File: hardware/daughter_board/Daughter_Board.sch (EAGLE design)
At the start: 75 parts, among them IC1 LMV358MMX, IC2 LMV358MMX, IC3 ATMEGA2560-16AU, IC4 ATMEGA16U2-MU, IC5 LMV358MMX, IC6 LP2985-33DBVR, IC7 LMV358IDGKR, IC8 LMV358MMX, IC9 LMV358MMX, J1 USB_MINI-B_SMT, T1 FDN340P, Y1 CSTCE16M0V53-R0 16MHZ, Y2 16MHz

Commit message: partial implementation of daughter board with rpi as bootloader
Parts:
- removed C10, C13: 1u, SmartPrj:C-EU0603-RND
- removed C11, C12, C6, C7, C8, C9: 100n, SmartPrj:C-EU0603-RND
- removed C14, C15: 22p, SmartPrj:C-EU0603-RND
- removed D2: CD1206-S01575, diode:DIODE-MINIMELF
- removed F1: MF-MSMF050-2 500mA, rcl:L-EUL1812
- removed GROUND, RESET-EN: (no value), jumper:SJ
- removed IC4: ATMEGA16U2-MU, SmartPrj:ATMEGA16U2-MU
- removed IC6: LP2985-33DBVR, SmartPrj:LP2985-XXDBVR33
- removed IC7: LMV358IDGKR, linear:LMV358MMX
- removed ICSP1: 3x2M, SmartPrj:PINHD-2X3
- removed JP2: (no value), adafruit:PINHD-1X12-CB
- removed JP5: 2x2M - NM, SmartPrj:PINHD-2X2
- removed ON: GREEN, led:LEDCHIP-LED0805
- removed RN1, RN10, RN11, RN3, RN4, RN6, RN8, RN9: 1k, resistor-dil:4R-NCAY16
- removed RN2: 22R, resistor-dil:4R-NCAY16
- removed RN5, RN7: 10K, resistor-dil:4R-NCAT16
- removed RX, TX: YELLOW, led:LEDCHIP-LED0805
- removed T1: FDN340P, zetex:PMOSSOT23
- removed Y2: 16MHz, SmartPrj:XTAL/S
- removed Z1, Z2: CG0603MLC-05E, varistor:VARISTORCN0603
- added J3, J4: (no value), SparkFun-Connectors:CONN_03
- added J5: (no value), SparkFun-Connectors:CONN_04
- added Q1: BSS138, SparkFun:MOSFET-NCHANNELSMD
- added R10, R11, R12, R3, R4, R5, R6, R7, R8, R9: 1k, resistor:R-EU_R0603
- added R13, R14, R15, R16, R17, R18, R19: 10k, resistor:R-EU_R0603
- added R20, R21: 10K, SparkFun:RESISTOR0603-RES
- J1: value USB_MINI-B_SMT -> (none); device SparkFun-Connectors:USB_MINI-B_SMT -> SparkFun-Connectors:CONN_03
- J2: device SparkFun-Connectors:CONN_04 -> SparkFun-Connectors:CONN_03
- L1: value BLM21 -> GREEN; device wuerth-elektronik:WE-CBF_0805 -> led:LEDCHIP-LED0805
- R2: value 1M -> 1k; device SmartPrj:R-EU_R0603 -> resistor:R-EU_R0603
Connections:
- removed net +3V3: C13.2, IC6.OUT, IC7B.-IN
- removed net 3V3_OUT_2: RPI-ZERO.17
- removed net 8PB4: IC4.(T1/PCINT4)PB4, JP5.1
- removed net 8PB5: IC4.(PCINT5)PB5, JP5.3
- removed net 8PB6: IC4.(PCINT6)PB6, JP5.2
- removed net 8PB7: IC4.(PCINT7/OC0A/OC1C)PB7, JP5.4
- removed net AREF: C3.1, IC3.AREF
- removed net CMP: C12.2, IC7B.+IN, RN5C.2, RN5D.2
- removed net D+: J1.D+, RN2A.2, Z2.2
- removed net D-: J1.D-, RN2D.2, Z1.2
- removed net DTR: C7.1, IC4.(CTS/HWB/AIN6/TO/INT7)PD7, RN3D.1
- removed net GATE_CMD: IC7B.OUT, T1.G
- removed net M8RXD: IC4.(TXD1/INT3)PD3, RN4B.2
- removed net M8TXD: IC4.(RXD1/AIN1/INT2)PD2, RN4A.2
- removed net MISO2: IC4.(PD0/MISO/PCINT3)PB3, ICSP1.1
- removed net MOSI2: IC4.(PDI/MOSI/PCINT2)PB2, ICSP1.4
- removed net N$54: RN4D.1, RX.A
- removed net N$55: RN4C.1, TX.A
- removed net PA0: IC3.(AD0)PA0
- removed net PA1: IC3.(AD1)PA1
- removed net PA2: IC3.(AD2)PA2
- removed net PA3: IC3.(AD3)PA3
- removed net PA4: IC3.(AD4)PA4
- removed net PA5: IC3.(AD5)PA5
- removed net PA6: IC3.(AD6)PA6
- removed net PA7: IC3.(AD7)PA7
- removed net PB0: IC3.(SS/PCINT0)PB0
- removed net PB4: IC3.(OC2A/PCINT4)PB4
- removed net PB5: IC3.(OC1A/PCINT5)PB5
- removed net PB6: IC3.(OC1B/PCINT6)PB6
- removed net PB7: IC3.(OC0A/OC1C/PCINT7)PB7
- removed net PC0: IC3.(A8)PC0
- removed net PC1: IC3.(A9)PC1
- removed net PC2: IC3.(A10)PC2
- removed net PC3: IC3.(A11)PC3
- removed net PC4: IC3.(A12)PC4
- removed net PC5: IC3.(A13)PC5
- removed net PC6: IC3.(A14)PC6
- removed net PC7: IC3.(A15)PC7
- removed net PD7: IC3.(T0)PD7
- removed net PF0: IC3.(ADC0)PF0
- removed net PF1: IC3.(ADC1)PF1
- removed net PF3: IC3.(ADC3)PF3
- removed net PF7: IC3.(ADC7/TDI)PF7
- removed net PG0: IC3.(WR)PG0
- removed net PG1: IC3.(RD)PG1
- removed net PG2: IC3.(ALE)PG2
- removed net PH3: IC3.PH3(OC4A)
- removed net PH4: IC3.PH4(OC4B)
- removed net PL0: IC3.PL0(ICP4)
- removed net PL1: IC3.PL1(ICP5)
- removed net PL2: IC3.PL2(T5)
- removed net PL3: IC3.PL3(OC5A)
- removed net PL4: IC3.PL4(OC5B)
- removed net PL5: IC3.PL5(OC5C)
- removed net PL6: IC3.PL6
- removed net PL7: IC3.PL7
- removed net RD+: IC4.D+, RN2A.1
- removed net RD-: IC4.D-, RN2D.1
- removed net RESET2: D2.A, IC4.RESET(PC1/DW), ICSP1.5, RN5B.2
- removed net RXL: IC4.(INT5/AIN3)PD4, RX.C
- removed net SCK2: IC4.(SCLK/PCINT1)PB1, ICSP1.3
- removed net TXL: IC4.(XCK/AIN4/PCINT12)PD5, TX.C
- removed net UGND: C10.2, GROUND.1, IC4.UGND, J1.GND, L1.1
- removed net USBVCC: C8.1, F1.1, IC4.UVCC, T1.D
- removed net USHIELD: J1.SHIELD, L1.2, Z1.1, Z2.1
- removed net VIN: RN5C.1
- removed net VUCAP: C10.1, IC4.UCAP
- removed net XT1: C14.1, IC4.XTAL1, R2.1, Y2.2
- removed net XT2: C15.1, IC4.XTAL2(PC0), R2.2, Y2.1
- removed net XVCC: F1.2, J1.VBUS
- new net HV: R21.1
- new net HV1: Q1.D, R21.2
- new net LV: Q1.G, R20.1
- new net LV1: Q1.S, R20.2
- net +5V: now also C3.1, J5.4, R12.1, R13.1; no longer C11.2, C6.1, C9.1, D2.C, IC4.AVCC, IC4.VCC, IC6.IN, IC6.ON/!OFF, IC7P.V+, ICSP1.2, J2.4, RN3A.1, RN4C.2, RN4D.2, RN5A.1, RN5B.1, T1.S
- net 3V3_OUT: now also R14.1, R15.1, R16.1, R17.1, R18.1, R19.1, RPI-ZERO.17; no longer RN7B.2, RN7C.2
- net GND: now also J1.1, J2.1, J3.1, J4.1, J5.2, L1.C; no longer C11.1, C12.1, C13.1, C14.2, C15.2, C6.2, C8.2, C9.2, GROUND.2, IC4.GND, IC4.PAD, IC6.GND, IC7P.V-, ICSP1.6, J2.2, JP2.12, JP2.3, JP2.4, JP2.9, ON.C, RN11A.1, RN11B.1, RN11C.1, RN11D.1, RN3D.2, RN5D.1
- net GPIO14: now also R14.2; no longer RN11A.2
- net GPIO15: now also R16.2; no longer RN11C.2
- net GPIO18: now also R17.2; no longer RN11D.2
- net GPIO4: now also R15.2; no longer RN11B.2
- net N$1: now also R3.2; no longer RN1A.2
- net N$10: now also R4.2; no longer RN6A.1
- net N$11: now also R5.2; no longer RN6B.1
- net N$12: now also R11.1; no longer RN9A.2
- net N$13: now also R7.2; no longer RN8B.2
- net N$14: now also R6.2; no longer RN8A.2
- net N$15: now also R10.1; no longer RN9B.2
- net N$16: now also R8.1; no longer RN10A.2
- net N$17: now also R9.1; no longer RN10B.2
- net N$18: now also R9.2; no longer RN10B.1
- net N$19: now also R8.2; no longer RN10A.1
- net N$2: now also R2.2; no longer RN1B.2
- net N$21: now also R11.2; no longer RN9A.1
- net N$22: now also R10.2; no longer RN9B.1
- net N$3: now also L1.A, R12.2; no longer ON.A, RN3A.2
- net N$4: now also R2.1; no longer RN1B.1
- net N$5: now also R7.1; no longer RN8B.1
- net N$6: now also R3.1; no longer RN1A.1
- net N$7: now also R6.1; no longer RN8A.1
- net N$8: now also R5.1; no longer RN6B.2
- net N$9: now also R4.1; no longer RN6A.2
- net PE0: now also J4.3; no longer JP2.10, RN4B.1
- net PE1: now also J4.2; no longer JP2.11, RN4A.1
- net PH5: now also IC1A.+IN, J5.1; no longer IC1B.+IN, J2.1
- net PH6: now also IC1B.+IN, J5.3; no longer IC1A.+IN, J2.3
- net RESET: now also R13.2; no longer C7.2, RESET-EN.1, RESET-EN.2, RN5A.2
- net RXD1: now also J3.3; no longer JP2.6
- net RXD2: now also J2.3; no longer JP2.7
- net RXD3: now also J1.3; no longer JP2.1
- net SCL: now also R18.2; no longer IC3.(SCL/INT0)PD0, RN7B.1
- net SDA: now also R19.2; no longer IC3.(SDA/INT1)PD1, RN7C.1
- net TXD1: now also J3.2; no longer JP2.5
- net TXD2: now also J2.2; no longer JP2.8
- net TXD3: now also J1.2; no longer JP2.2
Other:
- note removed: "USB boot En"
- moved on the sheet: C1, C2, C3, IC8A, L8, PAD1, PAD2, R1, R2, RESET

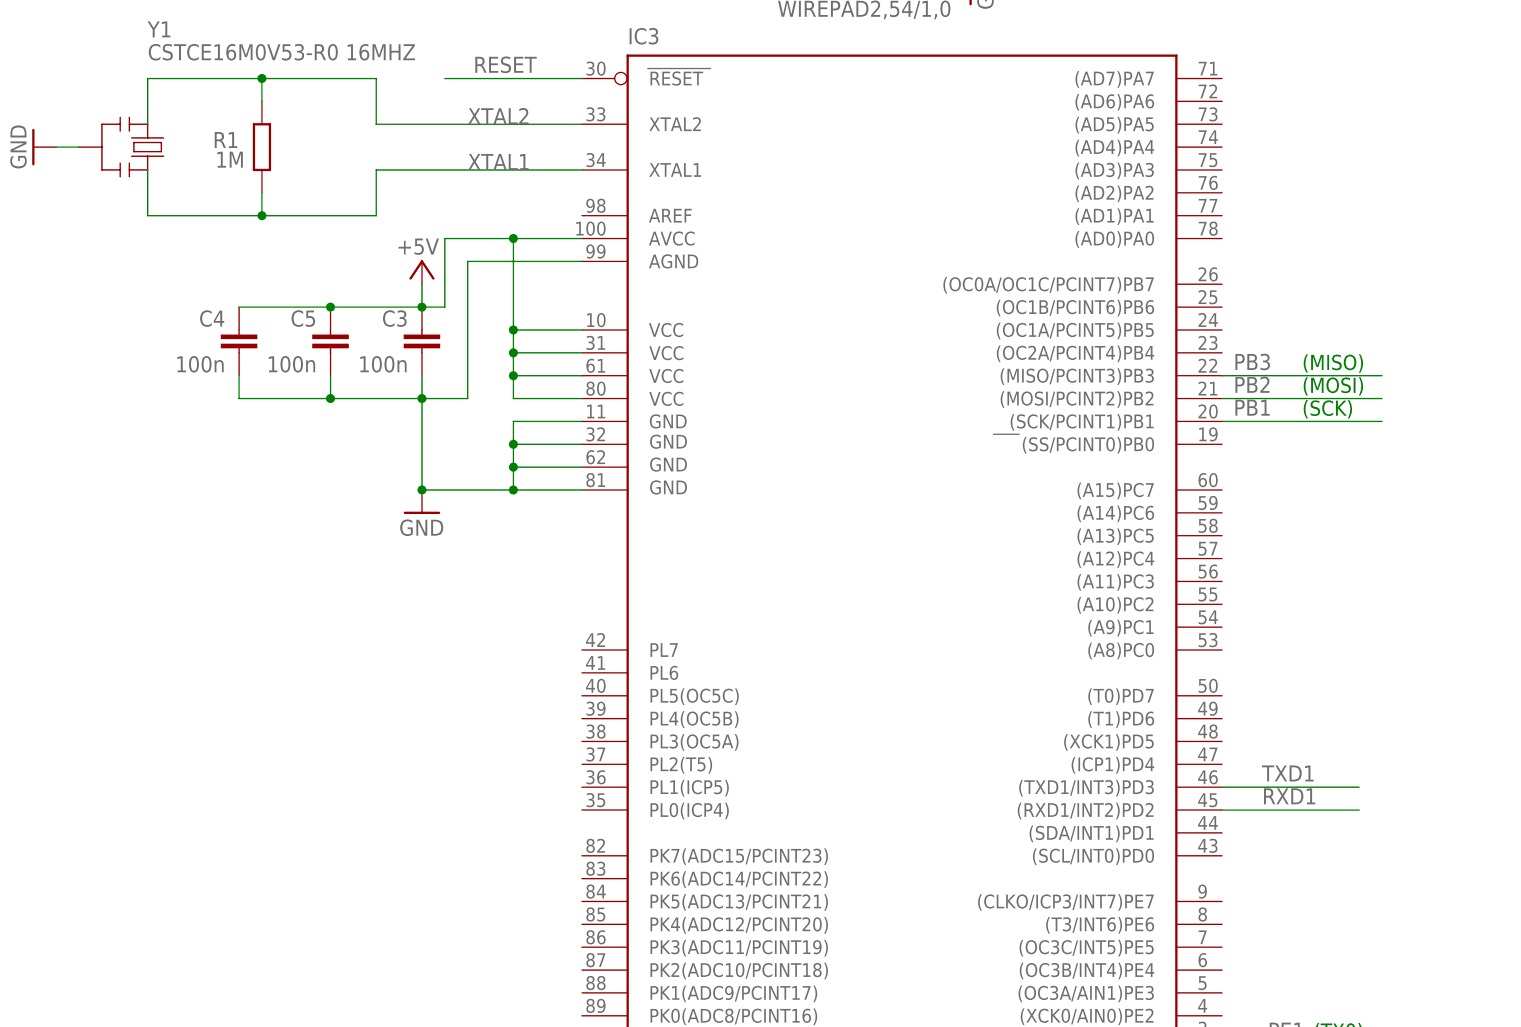
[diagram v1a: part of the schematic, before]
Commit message: route icsp header
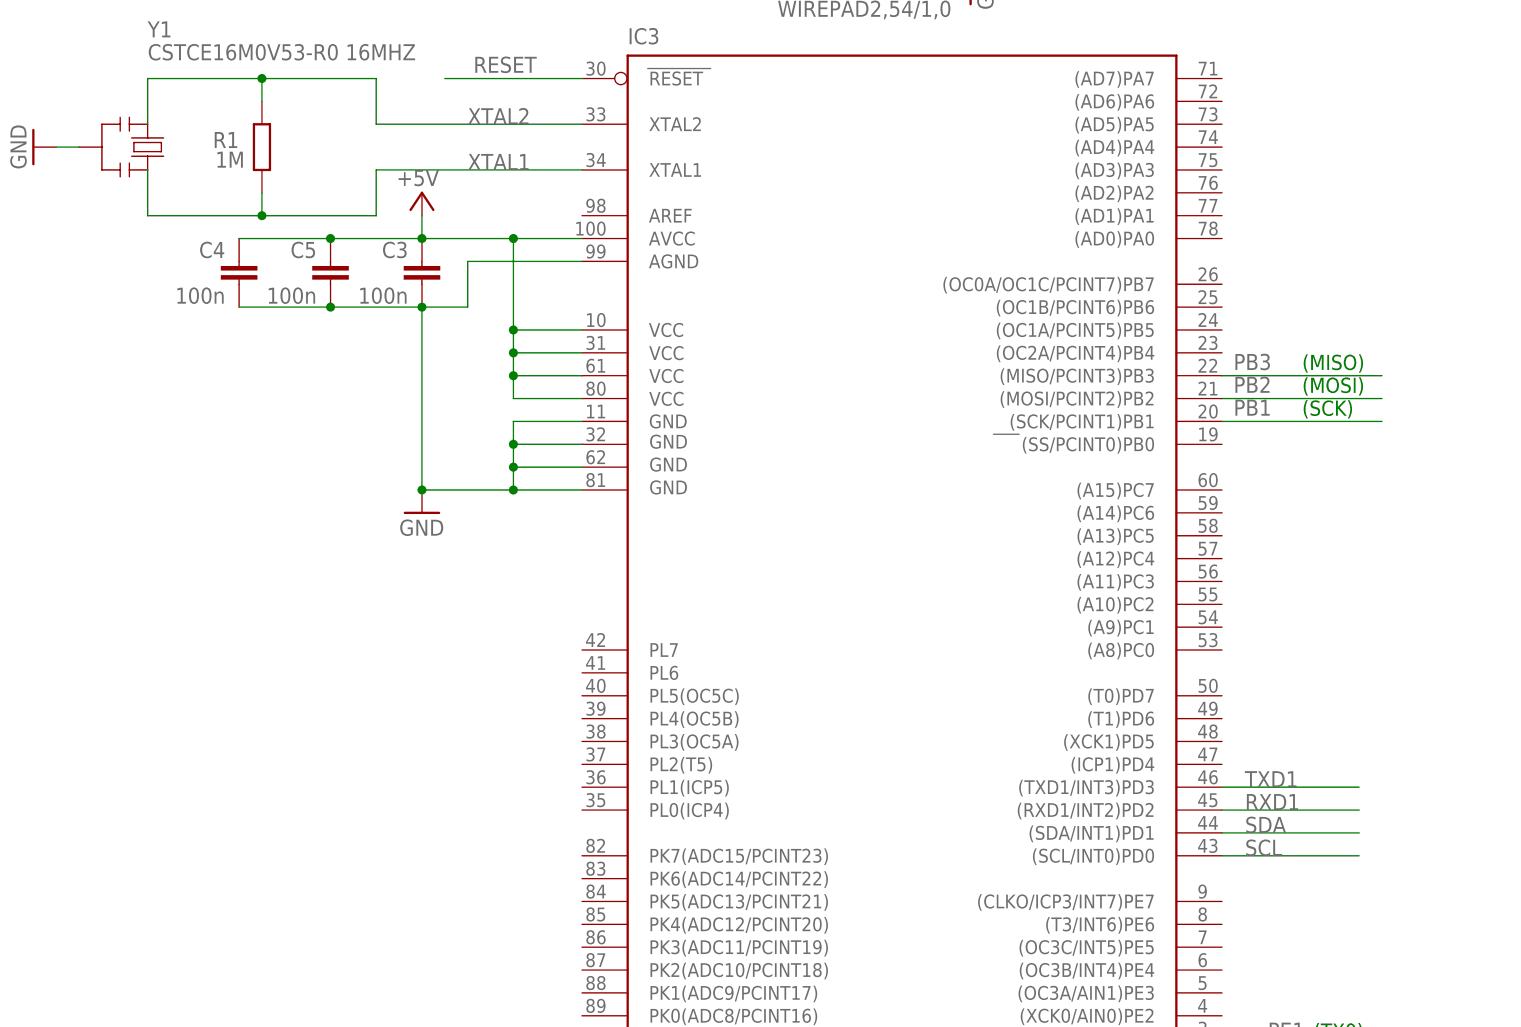
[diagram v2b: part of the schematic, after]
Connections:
- net SCL: now also IC3.(SCL/INT0)PD0
- net SDA: now also IC3.(SDA/INT1)PD1
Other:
- moved on the sheet: C3, C4, C5
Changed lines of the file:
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@@
 </instance>
 <instance part="GND6" gate="1" x="2.54" y="15.24"/>
-<instance part="P+3" gate="1" x="86.36" y="228.6" smashed="yes">
-<attribute name="VALUE" x="88.265" y="231.14" size="1.778" layer="96" rot="R180"/>
+<instance part="P+3" gate="1" x="86.36" y="236.22" smashed="yes">
+<attribute name="VALUE" x="88.265" y="238.76" size="1.778" layer="96" rot="R180"/>
 </instance>
 <instance part="GND2" gate="1" x="86.36" y="200.66" smashed="yes">
@@
 <attribute name="VALUE" x="109.22" y="93.98" size="1.778" layer="96"/>
 </instance>
-<instance part="C5" gate="G$1" x="76.2" y="220.98" smashed="yes" rot="MR0">
-<attribute name="NAME" x="74.676" y="221.361" size="1.778" layer="95" rot="MR0"/>
-<attribute name="VALUE" x="74.676" y="216.281" size="1.778" layer="96" rot="MR0"/>
-</instance>
-<instance part="C4" gate="G$1" x="66.04" y="220.98" smashed="yes" rot="MR0">
-<attribute name="NAME" x="64.516" y="221.361" size="1.778" layer="95" rot="MR0"/>
-<attribute name="VALUE" x="64.516" y="216.281" size="1.778" layer="96" rot="MR0"/>
+<instance part="C5" gate="G$1" x="76.2" y="228.6" smashed="yes" rot="MR0">
+<attribute name="NAME" x="74.676" y="228.981" size="1.778" layer="95" rot="MR0"/>
+<attribute name="VALUE" x="74.676" y="223.901" size="1.778" layer="96" rot="MR0"/>
+</instance>
+<instance part="C4" gate="G$1" x="66.04" y="228.6" smashed="yes" rot="MR0">
+<attribute name="NAME" x="64.516" y="228.981" size="1.778" layer="95" rot="MR0"/>
+<attribute name="VALUE" x="64.516" y="223.901" size="1.778" layer="96" rot="MR0"/>
 </instance>
 <instance part="C1" gate="G$1" x="238.76" y="274.32" rot="MR0"/>
@@
 <instance part="R18" gate="G$1" x="287.02" y="129.54" rot="R270"/>
 <instance part="R19" gate="G$1" x="294.64" y="129.54" rot="R270"/>
-<instance part="C3" gate="G$1" x="86.36" y="220.98" smashed="yes" rot="MR0">
-<attribute name="NAME" x="84.836" y="221.361" size="1.778" layer="95" rot="MR0"/>
-<attribute name="VALUE" x="84.836" y="216.281" size="1.778" layer="96" rot="MR0"/>
+<instance part="C3" gate="G$1" x="86.36" y="228.6" smashed="yes" rot="MR0">
+<attribute name="NAME" x="84.836" y="228.981" size="1.778" layer="95" rot="MR0"/>
+<attribute name="VALUE" x="84.836" y="223.901" size="1.778" layer="96" rot="MR0"/>
 </instance>
 <instance part="J1" gate="J$1" x="243.84" y="218.44"/>
@@
 </segment>
 <segment>
-<wire x1="86.36" y1="203.2" x2="86.36" y2="213.36" width="0.1524" layer="91"/>
-<wire x1="76.2" y1="215.9" x2="76.2" y2="213.36" width="0.1524" layer="91"/>
-<wire x1="76.2" y1="213.36" x2="86.36" y2="213.36" width="0.1524" layer="91"/>
-<wire x1="76.2" y1="213.36" x2="66.04" y2="213.36" width="0.1524" layer="91"/>
-<wire x1="66.04" y1="213.36" x2="66.04" y2="215.9" width="0.1524" layer="91"/>
+<wire x1="86.36" y1="203.2" x2="86.36" y2="223.52" width="0.1524" layer="91"/>
+<wire x1="76.2" y1="223.52" x2="86.36" y2="223.52" width="0.1524" layer="91"/>
+<wire x1="76.2" y1="223.52" x2="66.04" y2="223.52" width="0.1524" layer="91"/>
 <wire x1="104.14" y1="228.6" x2="91.44" y2="228.6" width="0.1524" layer="91"/>
-<wire x1="91.44" y1="228.6" x2="91.44" y2="213.36" width="0.1524" layer="91"/>
-<wire x1="91.44" y1="213.36" x2="86.36" y2="213.36" width="0.1524" layer="91"/>
+<wire x1="91.44" y1="228.6" x2="91.44" y2="223.52" width="0.1524" layer="91"/>
+<wire x1="91.44" y1="223.52" x2="86.36" y2="223.52" width="0.1524" layer="91"/>
 <wire x1="104.14" y1="203.2" x2="96.52" y2="203.2" width="0.1524" layer="91"/>
 <wire x1="96.52" y1="203.2" x2="86.36" y2="203.2" width="0.1524" layer="91"/>
@@
 <wire x1="104.14" y1="208.28" x2="96.52" y2="208.28" width="0.1524" layer="91"/>
 <wire x1="104.14" y1="205.74" x2="96.52" y2="205.74" width="0.1524" layer="91"/>
-<junction x="86.36" y="213.36"/>
-<junction x="76.2" y="213.36"/>
+<junction x="86.36" y="223.52"/>
+<junction x="76.2" y="223.52"/>
 <junction x="86.36" y="203.2"/>
 <junction x="96.52" y="203.2"/>
@@
 <pinref part="IC3" gate="1" pin="GND2"/>
 <pinref part="C3" gate="G$1" pin="2"/>
-<wire x1="86.36" y1="213.36" x2="86.36" y2="215.9" width="0.1524" layer="91"/>
 </segment>
 <segment>
@@
 </segment>
 <segment>
-<wire x1="86.36" y1="226.06" x2="86.36" y2="223.52" width="0.1524" layer="91"/>
+<wire x1="86.36" y1="233.68" x2="86.36" y2="231.14" width="0.1524" layer="91"/>
 <wire x1="104.14" y1="231.14" x2="96.52" y2="231.14" width="0.1524" layer="91"/>
-<wire x1="96.52" y1="231.14" x2="88.9" y2="231.14" width="0.1524" layer="91"/>
-<wire x1="88.9" y1="231.14" x2="88.9" y2="223.52" width="0.1524" layer="91"/>
-<wire x1="76.2" y1="223.52" x2="66.04" y2="223.52" width="0.1524" layer="91"/>
+<wire x1="96.52" y1="231.14" x2="86.36" y2="231.14" width="0.1524" layer="91"/>
+<wire x1="76.2" y1="231.14" x2="66.04" y2="231.14" width="0.1524" layer="91"/>
 <wire x1="104.14" y1="213.36" x2="96.52" y2="213.36" width="0.1524" layer="91"/>
 <wire x1="96.52" y1="213.36" x2="96.52" y2="215.9" width="0.1524" layer="91"/>
@@
 <wire x1="104.14" y1="218.44" x2="96.52" y2="218.44" width="0.1524" layer="91"/>
 <wire x1="104.14" y1="215.9" x2="96.52" y2="215.9" width="0.1524" layer="91"/>
-<wire x1="76.2" y1="223.52" x2="86.36" y2="223.52" width="0.1524" layer="91"/>
-<wire x1="86.36" y1="223.52" x2="88.9" y2="223.52" width="0.1524" layer="91"/>
-<junction x="76.2" y="223.52"/>
+<wire x1="76.2" y1="231.14" x2="86.36" y2="231.14" width="0.1524" layer="91"/>
+<junction x="76.2" y="231.14"/>
 <junction x="96.52" y="220.98"/>
 <junction x="96.52" y="231.14"/>
 <junction x="96.52" y="218.44"/>
 <junction x="96.52" y="215.9"/>
-<junction x="86.36" y="223.52"/>
+<junction x="86.36" y="231.14"/>
 <pinref part="P+3" gate="1" pin="+5V"/>
 <pinref part="IC3" gate="1" pin="AVCC"/>
@@
 <label x="-10.16" y="68.58" size="1.778" layer="95"/>
 </segment>
+<segment>
+<pinref part="IC3" gate="1" pin="(SDA/INT1)PD1"/>
+<wire x1="175.26" y1="165.1" x2="190.5" y2="165.1" width="0.1524" layer="91"/>
+<label x="177.8" y="165.1" size="1.778" layer="95"/>
+</segment>
 </net>
 <net name="SCL" class="0">
@@
 <wire x1="10.16" y1="66.04" x2="2.54" y2="66.04" width="0.1524" layer="91"/>
 <label x="-10.16" y="66.04" size="1.778" layer="95"/>
+</segment>
+<segment>
+<pinref part="IC3" gate="1" pin="(SCL/INT0)PD0"/>
+<wire x1="175.26" y1="162.56" x2="190.5" y2="162.56" width="0.1524" layer="91"/>
+<label x="177.8" y="162.56" size="1.778" layer="95"/>
 </segment>
 </net>
@@
 <segment>
 <wire x1="190.5" y1="167.64" x2="175.26" y2="167.64" width="0.1524" layer="91"/>
-<label x="179.705" y="168.275" size="1.778" layer="95"/>
 <pinref part="IC3" gate="1" pin="(RXD1/INT2)PD2"/>
+<label x="177.8" y="167.64" size="1.778" layer="95"/>
 </segment>
 <segment>
@@
 <segment>
 <wire x1="190.5" y1="170.18" x2="175.26" y2="170.18" width="0.1524" layer="91"/>
-<label x="179.705" y="170.815" size="1.778" layer="95"/>
 <pinref part="IC3" gate="1" pin="(TXD1/INT3)PD3"/>
-</segment>
-<segment>
+<label x="177.8" y="170.18" size="1.778" layer="95"/>
+</segment>
+<segment>
